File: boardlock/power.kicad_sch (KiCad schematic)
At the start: 24 parts, among them U6 TPS630701RNMR

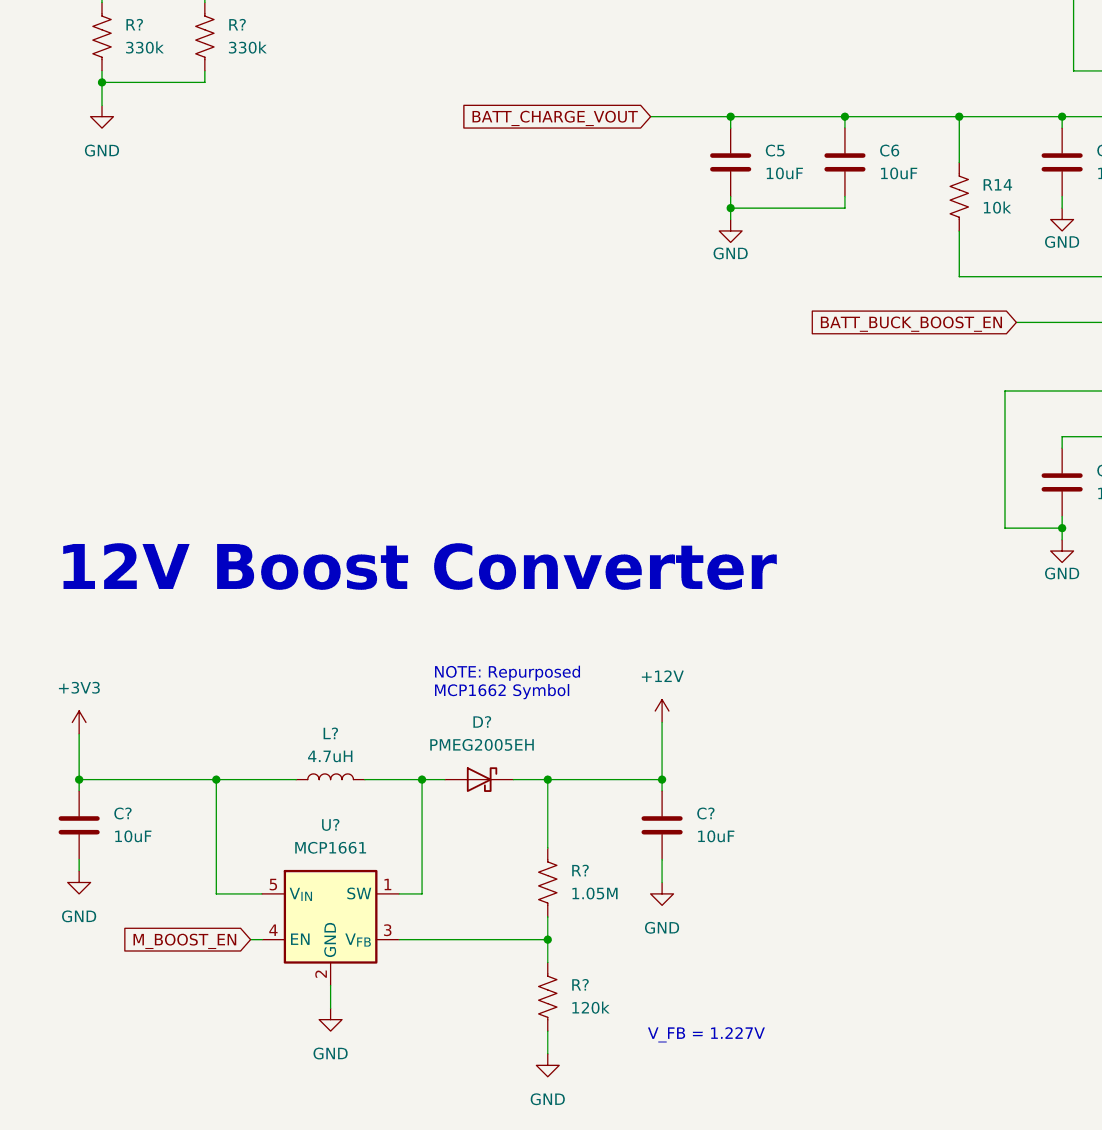
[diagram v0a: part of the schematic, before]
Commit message: footprint updates
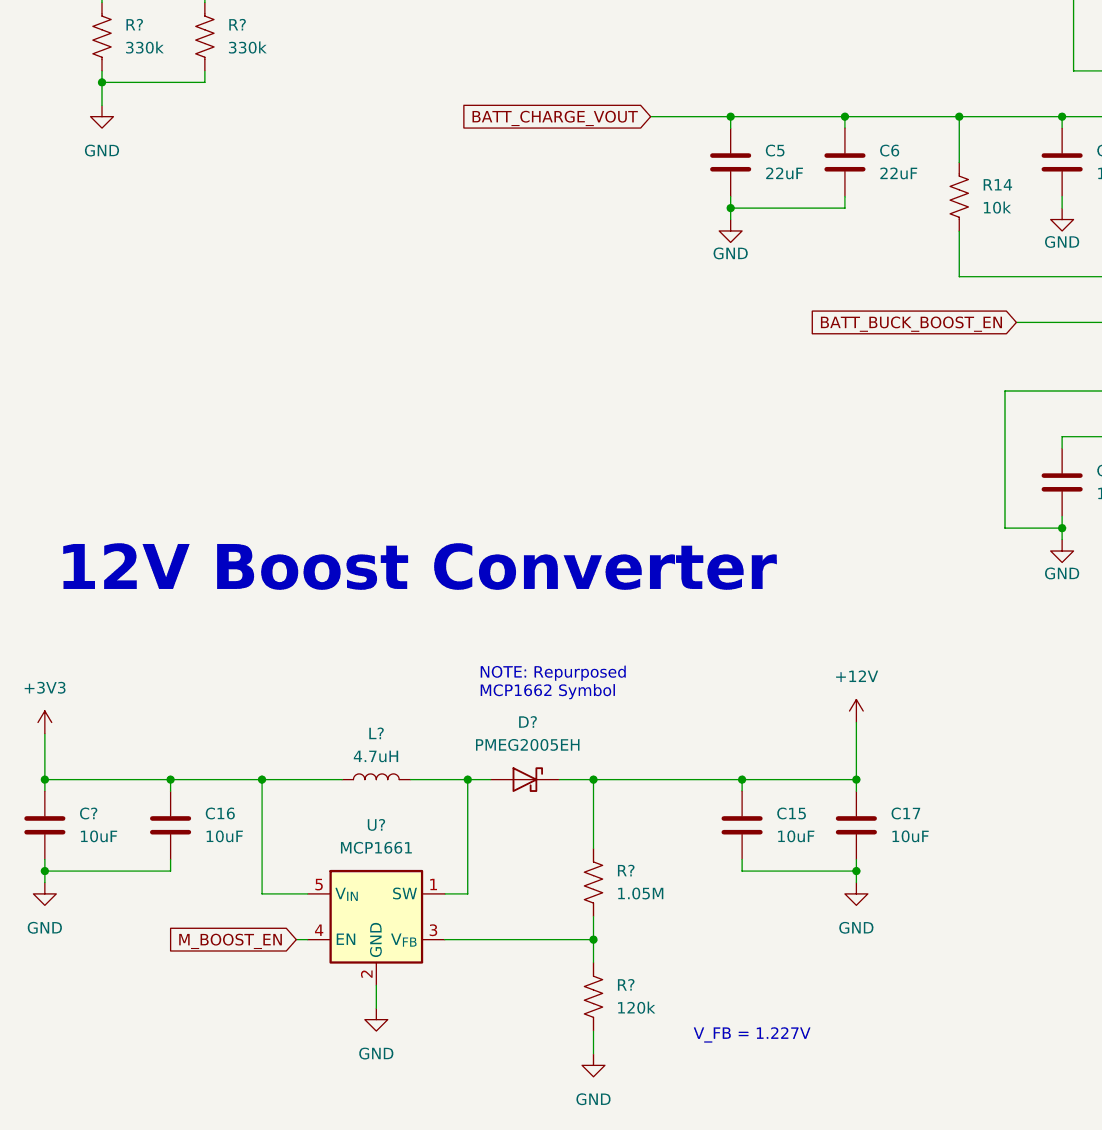
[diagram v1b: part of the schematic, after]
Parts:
- removed C?: 10uF, Capacitor_SMD:C_0805_2012Metric_Pad1.18x1.45mm_HandSolder, symbol Device:C
- added C15, C17: 10uF, Capacitor_SMD:C_1206_3216Metric_Pad1.33x1.80mm_HandSolder, symbol Device:C
- added C16: 10uF, Capacitor_SMD:C_0805_2012Metric_Pad1.18x1.45mm_HandSolder, symbol Device:C
- C5, C6: value 10uF -> 22uF
- L?: footprint (none) -> Inductor_SMD:L_Coilcraft_XxL4020
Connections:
- net +12V: now also C15.1, C17.1
- net +3V3: now also C16.1
- net GND: now also C15.2, C16.2, C17.2
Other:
- moved on the sheet: C?, D?, L?, R?, U?

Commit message: footprint work
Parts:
- gave numbers to parts that had none: 9
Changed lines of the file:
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@@
   (symbol (lib_id "Device:R_US") (at 87.63 153.67 0) (unit 1)
     (in_bom yes) (on_board yes) (dnp no) (fields_autoplaced)
-    (property "Reference" "R?" (at 90.17 152.4 0)
+    (property "Reference" "R54" (at 90.17 152.4 0)
       (effects (font (size 1.27 1.27)) (justify left))
     )
@@
       (project "boardlock"
         (path "/e1fc29ce-837e-4062-84d8-c7e423f9eab9/5801071c-337d-449a-92e5-5afeb5febc0d"
-          (reference "R?") (unit 1)
+          (reference "R54") (unit 1)
         )
         (path "/e1fc29ce-837e-4062-84d8-c7e423f9eab9/1eb676fb-9e7a-4e01-ba1e-2eff94d7b66e"
@@
   (symbol (lib_id "Device:R_US") (at 33.02 59.69 0) (unit 1)
     (in_bom yes) (on_board yes) (dnp no) (fields_autoplaced)
-    (property "Reference" "R?" (at 35.56 58.42 0)
+    (property "Reference" "R52" (at 35.56 58.42 0)
       (effects (font (size 1.27 1.27)) (justify left))
     )
@@
       (project "boardlock"
         (path "/e1fc29ce-837e-4062-84d8-c7e423f9eab9/5801071c-337d-449a-92e5-5afeb5febc0d"
-          (reference "R?") (unit 1)
+          (reference "R52") (unit 1)
         )
         (path "/e1fc29ce-837e-4062-84d8-c7e423f9eab9/a05f4dcd-7a18-4529-a05e-43353e81fbf8"
@@
   (symbol (lib_id "Device:C") (at 26.67 147.32 0) (unit 1)
     (in_bom yes) (on_board yes) (dnp no) (fields_autoplaced)
-    (property "Reference" "C?" (at 30.48 146.05 0)
+    (property "Reference" "C29" (at 30.48 146.05 0)
       (effects (font (size 1.27 1.27)) (justify left))
     )
@@
       (project "boardlock"
         (path "/e1fc29ce-837e-4062-84d8-c7e423f9eab9/5801071c-337d-449a-92e5-5afeb5febc0d"
-          (reference "C?") (unit 1)
+          (reference "C29") (unit 1)
         )
         (path "/e1fc29ce-837e-4062-84d8-c7e423f9eab9/1eb676fb-9e7a-4e01-ba1e-2eff94d7b66e"
@@
   (symbol (lib_id "Device:L") (at 63.5 142.24 90) (unit 1)
     (in_bom yes) (on_board yes) (dnp no)
-    (property "Reference" "L?" (at 63.5 137.16 90)
+    (property "Reference" "L2" (at 63.5 137.16 90)
       (effects (font (size 1.27 1.27)))
     )
@@
       (project "boardlock"
         (path "/e1fc29ce-837e-4062-84d8-c7e423f9eab9/5801071c-337d-449a-92e5-5afeb5febc0d"
-          (reference "L?") (unit 1)
+          (reference "L2") (unit 1)
         )
         (path "/e1fc29ce-837e-4062-84d8-c7e423f9eab9/1eb676fb-9e7a-4e01-ba1e-2eff94d7b66e"
@@
   (symbol (lib_id "Device:R_US") (at 33.02 46.99 0) (unit 1)
     (in_bom yes) (on_board yes) (dnp no) (fields_autoplaced)
-    (property "Reference" "R?" (at 35.56 45.72 0)
+    (property "Reference" "R51" (at 35.56 45.72 0)
       (effects (font (size 1.27 1.27)) (justify left))
     )
@@
       (project "boardlock"
         (path "/e1fc29ce-837e-4062-84d8-c7e423f9eab9/5801071c-337d-449a-92e5-5afeb5febc0d"
-          (reference "R?") (unit 1)
+          (reference "R51") (unit 1)
         )
         (path "/e1fc29ce-837e-4062-84d8-c7e423f9eab9/a05f4dcd-7a18-4529-a05e-43353e81fbf8"
@@
   (symbol (lib_id "Driver_LED:MCP1662-xOT") (at 63.5 157.48 0) (unit 1)
     (in_bom yes) (on_board yes) (dnp no) (fields_autoplaced)
-    (property "Reference" "U?" (at 63.5 147.32 0)
+    (property "Reference" "U8" (at 63.5 147.32 0)
       (effects (font (size 1.27 1.27)))
     )
@@
       (project "boardlock"
         (path "/e1fc29ce-837e-4062-84d8-c7e423f9eab9/5801071c-337d-449a-92e5-5afeb5febc0d"
+          (reference "U8") (unit 1)
+        )
+        (path "/e1fc29ce-837e-4062-84d8-c7e423f9eab9/1eb676fb-9e7a-4e01-ba1e-2eff94d7b66e"
           (reference "U?") (unit 1)
         )
-        (path "/e1fc29ce-837e-4062-84d8-c7e423f9eab9/1eb676fb-9e7a-4e01-ba1e-2eff94d7b66e"
-          (reference "U?") (unit 1)
-        )
       )
     )
@@
   (symbol (lib_id "Device:R_US") (at 87.63 166.37 0) (unit 1)
     (in_bom yes) (on_board yes) (dnp no) (fields_autoplaced)
-    (property "Reference" "R?" (at 90.17 165.1 0)
+    (property "Reference" "R55" (at 90.17 165.1 0)
       (effects (font (size 1.27 1.27)) (justify left))
     )
@@
       (project "boardlock"
         (path "/e1fc29ce-837e-4062-84d8-c7e423f9eab9/5801071c-337d-449a-92e5-5afeb5febc0d"
-          (reference "R?") (unit 1)
+          (reference "R55") (unit 1)
         )
         (path "/e1fc29ce-837e-4062-84d8-c7e423f9eab9/1eb676fb-9e7a-4e01-ba1e-2eff94d7b66e"
@@
   (symbol (lib_id "Device:R_US") (at 44.45 59.69 0) (unit 1)
     (in_bom yes) (on_board yes) (dnp no)
-    (property "Reference" "R?" (at 46.99 58.42 0)
+    (property "Reference" "R53" (at 46.99 58.42 0)
       (effects (font (size 1.27 1.27)) (justify left))
     )
@@
       (project "boardlock"
         (path "/e1fc29ce-837e-4062-84d8-c7e423f9eab9/5801071c-337d-449a-92e5-5afeb5febc0d"
-          (reference "R?") (unit 1)
+          (reference "R53") (unit 1)
         )
         (path "/e1fc29ce-837e-4062-84d8-c7e423f9eab9/a05f4dcd-7a18-4529-a05e-43353e81fbf8"
@@
   (symbol (lib_id "Diode:PMEG2005EH") (at 80.01 142.24 0) (mirror y) (unit 1)
     (in_bom yes) (on_board yes) (dnp no)
-    (property "Reference" "D?" (at 80.3275 135.89 0)
+    (property "Reference" "D1" (at 80.3275 135.89 0)
       (effects (font (size 1.27 1.27)))
     )
@@
       (project "boardlock"
         (path "/e1fc29ce-837e-4062-84d8-c7e423f9eab9/5801071c-337d-449a-92e5-5afeb5febc0d"
-          (reference "D?") (unit 1)
-        )
-        (path "/e1fc29ce-837e-4062-84d8-c7e423f9eab9/1eb676fb-9e7a-4e01-ba1e-2eff94d7b66e"
+          (reference "D1") (unit 1)
+        )
+        (path "/e1fc29ce-837e-4062-84d8-c7e423f9eab9/1eb676fb-9e7a-4e01-ba1e-2eff94d7b66e"

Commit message: changes
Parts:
- C7, C9: footprint Resistor_SMD:R_0603_1608Metric_Pad0.98x0.95mm_HandSolder -> Capacitor_SMD:C_0603_1608Metric_Pad1.08x0.95mm_HandSolder
- C8: footprint Resistor_SMD:R_0402_1005Metric_Pad0.72x0.64mm_HandSolder -> Capacitor_SMD:C_0603_1608Metric_Pad1.08x0.95mm_HandSolder
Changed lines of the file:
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@@
       (effects (font (size 1.27 1.27)) (justify left))
     )
-    (property "Footprint" "Resistor_SMD:R_0402_1005Metric_Pad0.72x0.64mm_HandSolder" (at 140.6652 113.03 0)
+    (property "Footprint" "Capacitor_SMD:C_0603_1608Metric_Pad1.08x0.95mm_HandSolder" (at 140.6652 113.03 0)
       (effects (font (size 1.27 1.27)) hide)
     )
@@
       (effects (font (size 1.27 1.27)) (justify left))
     )
-    (property "Footprint" "Resistor_SMD:R_0603_1608Metric_Pad0.98x0.95mm_HandSolder" (at 140.6652 77.47 0)
+    (property "Footprint" "Capacitor_SMD:C_0603_1608Metric_Pad1.08x0.95mm_HandSolder" (at 140.6652 77.47 0)
       (effects (font (size 1.27 1.27)) hide)
     )
@@
       (effects (font (size 1.27 1.27)) (justify left))
     )
-    (property "Footprint" "Resistor_SMD:R_0603_1608Metric_Pad0.98x0.95mm_HandSolder" (at 192.7352 77.47 0)
-      (effects (font (size 1.27 1.27)) hide)
-    )
+    (property "Footprint" "Capacitor_SMD:C_0603_1608Metric_Pad1.08x0.95mm_HandSolder" (at 192.7352 77.47 0)
+      (effects (font (size 1.27 1.27)) hide)
+    )

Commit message: added inductor footprints
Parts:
- L1: footprint (none) -> DR74-1R5-R:DR74
- L2: footprint Inductor_SMD:L_Coilcraft_XxL4020 -> B82462G4472M000:IND_EPCOS_B82462G4_EPC
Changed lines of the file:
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@@
       (effects (font (size 1.27 1.27)))
     )
-    (property "Footprint" "Inductor_SMD:L_Coilcraft_XxL4020" (at 63.5 142.24 0)
-      (effects (font (size 1.27 1.27)) hide)
-    )
-    (property "Datasheet" "https://www.coilcraft.com/getmedia/76c9c081-4945-4c85-9129-9356e1ad6734/xgl4020.pdf" (at 63.5 142.24 0)
+    (property "Footprint" "B82462G4472M000:IND_EPCOS_B82462G4_EPC" (at 63.5 142.24 0)
+      (effects (font (size 1.27 1.27)) hide)
+    )
+    (property "Datasheet" "" (at 63.5 142.24 0)
       (effects (font (size 1.27 1.27)) hide)
     )
@@
       (effects (font (size 1.27 1.27)))
     )
-    (property "Footprint" "" (at 165.1 45.72 0)
-      (effects (font (size 1.27 1.27)) hide)
-    )
+    (property "Footprint" "DR74-1R5-R:DR74" (at 165.1 45.72 0)
+      (effects (font (size 1.27 1.27)) hide)
+    )

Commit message: footprints finished for now
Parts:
- R11: footprint (none) -> Resistor_SMD:R_0805_2012Metric_Pad1.20x1.40mm_HandSolder
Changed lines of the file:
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@@
       (effects (font (size 1.27 1.27)) (justify left))
     )
-    (property "Footprint" "" (at 221.996 84.074 90)
+    (property "Footprint" "Resistor_SMD:R_0805_2012Metric_Pad1.20x1.40mm_HandSolder" (at 221.996 84.074 90)
       (effects (font (size 1.27 1.27)) hide)
     )

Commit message: more pcb stuff
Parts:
- renumbered C10 to C11, C11 to C12, C12 to C13, C5 to C14, C6 to C15, C7 to C16, C9 to C17, C8 to C18, C29 to C19, C16 to C20, C15 to C21, C17 to C22, D1 to D2, R51 to R26, R52 to R27, R53 to R28, R9 to R29, R14 to R30, R11 to R31, R10 to R32, R54 to R33, R55 to R34, U8 to U7
